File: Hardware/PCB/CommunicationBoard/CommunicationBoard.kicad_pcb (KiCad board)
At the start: 4 copper layers, 60 x 60 mm, 54 parts, among them J1 SWD, J2 Conn_01x07, J3 Conn_01x07, J4 Conn_01x07, J6 USB_C_Receptacle_USB2.0, J7 TWELITER, SW1 nRF_RESET, SW2 nRF_DFU, SW3 TWE_CLEAR, SW4 TWE_RESET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

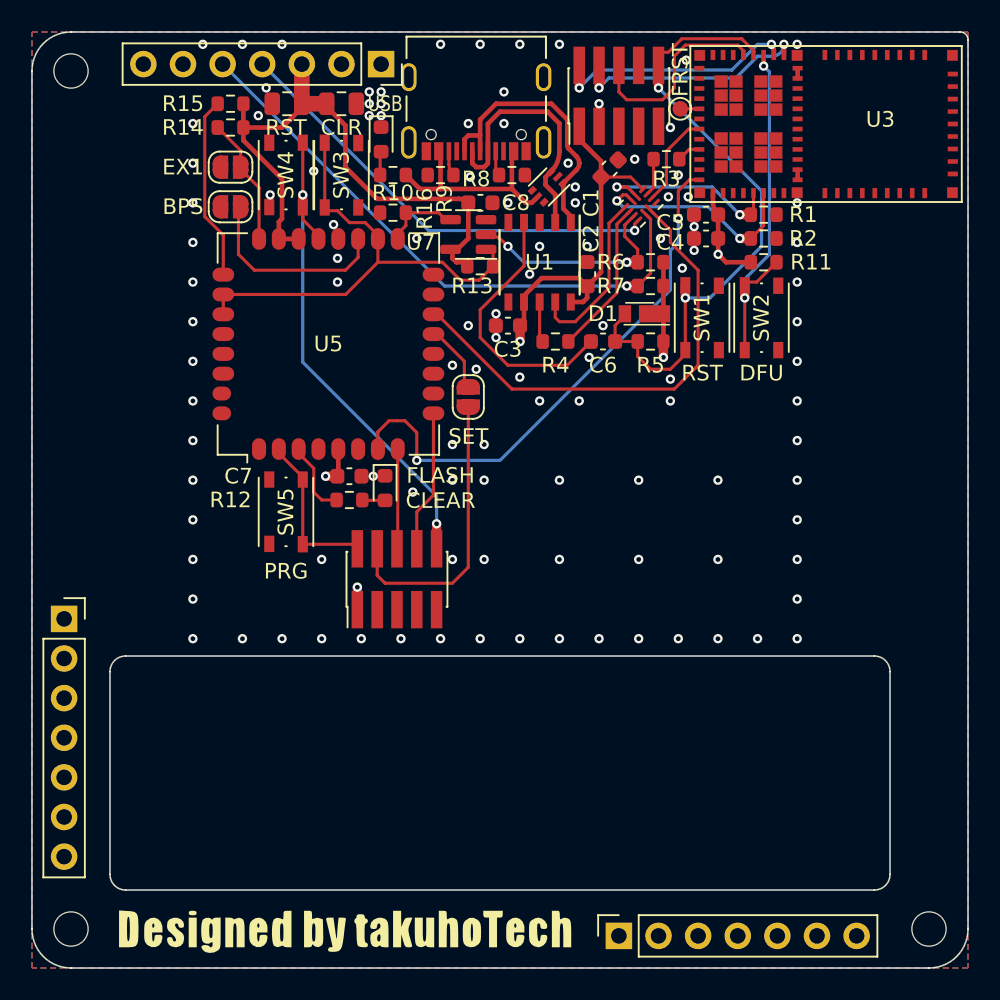
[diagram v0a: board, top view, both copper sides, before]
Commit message: 無線モジュールのビア置き終了、ひとまず完成
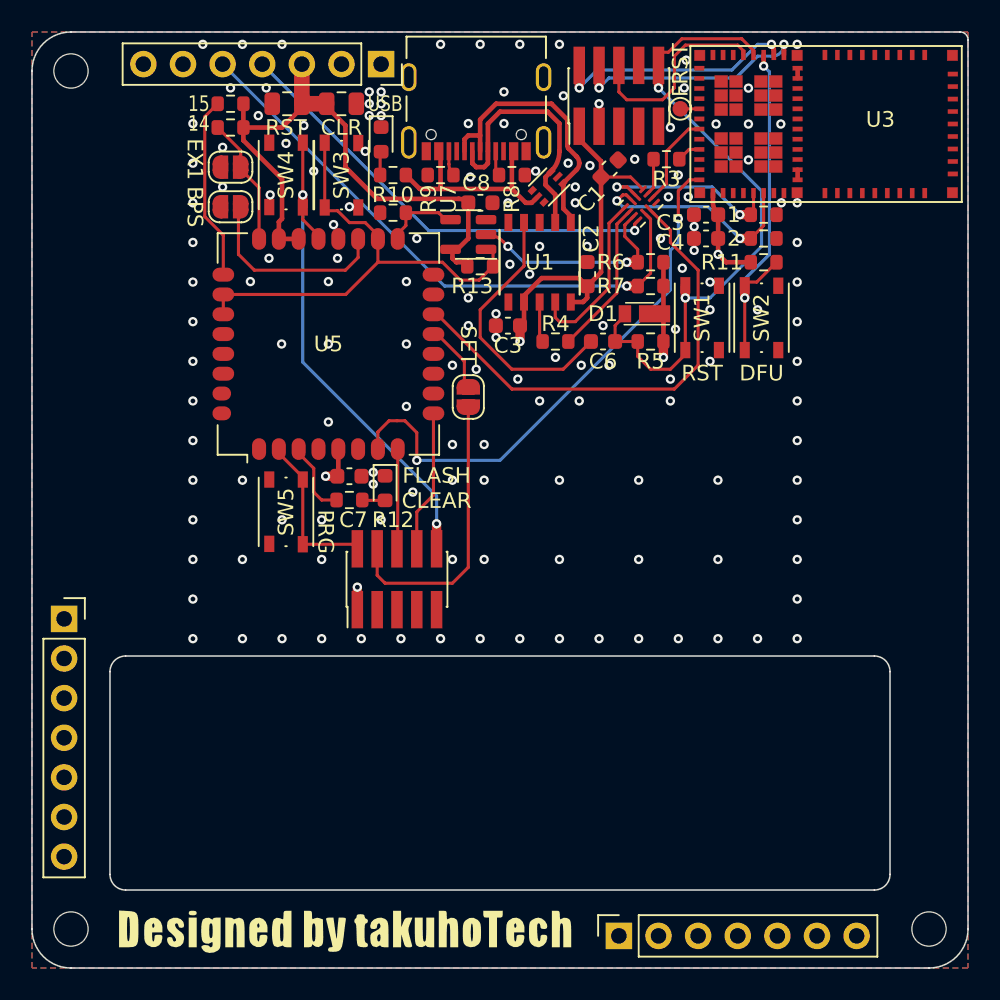
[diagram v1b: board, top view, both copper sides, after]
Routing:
- net GND: vias 111 -> 151
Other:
- board text added: "1"
- board text added: "14"
- board text added: "15"
- board text added: "2"
- board text added: "3V3"
- board text added: "GND"
- board text added: "NC"
- board text added: "RXIN"
- board text added: "TXOUT"

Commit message: Add MediaBoard
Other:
- board text added: "MEM CLR"
- board text removed: "FLASH CLEAR"
- board text removed: "LoRaアンテナのゲインの回転軸"
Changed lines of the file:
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@@
     (grid_origin 145 100)
     (pcbplotparams
-      (layerselection 0x00010a0_7ffffff8)
+      (layerselection 0x00010fc_ffffffff)
       (disableapertmacros false)
-      (usegerberextensions false)
-      (usegerberattributes true)
-      (usegerberadvancedattributes true)
-      (creategerberjobfile true)
+      (usegerberextensions true)
+      (usegerberattributes false)
+      (usegerberadvancedattributes false)
+      (creategerberjobfile false)
       (svguseinch false)
       (svgprecision 6)
-      (excludeedgelayer false)
+      (excludeedgelayer true)
       (plotframeref false)
       (viasonmask false)
       (mode 1)
-      (useauxorigin false)
+      (useauxorigin true)
       (hpglpennumber 1)
       (hpglpenspeed 20)
@@
       (plotinvisibletext false)
       (sketchpadsonfab false)
-      (subtractmaskfromsilk false)
-      (outputformat 5)
+      (subtractmaskfromsilk true)
+      (outputformat 1)
       (mirror false)
       (drillshape 0)
       (scaleselection 1)
-      (outputdirectory "")
+      (outputdirectory "gerber/")
     )
   )
@@
     (property "Sheetname" "")
     (attr smd)
-    (fp_text reference "C6" (at 0 1.27) (layer "F.SilkS")
+    (fp_text reference "C6" (at -1.905 -1.143) (layer "F.SilkS")
       (effects (font (size 1 1) (thickness 0.15)))
     )
@@
     (property "Sheetname" "")
     (attr smd)
-    (fp_text reference "R4" (at 0 -1.143) (layer "F.SilkS")
+    (fp_text reference "R4" (at -0.762 -1.143) (layer "F.SilkS")
       (effects (font (size 1 1) (thickness 0.15)))
     )
@@
     (property "Sheetname" "")
     (attr smd)
-    (fp_text reference "D1" (at 2.352 0) (layer "F.SilkS")
+    (fp_text reference "D1" (at 2.352 0.762) (layer "F.SilkS") hide
       (effects (font (size 1 1) (thickness 0.15)))
     )
@@
     (property "Sheetname" "")
     (attr smd)
-    (fp_text reference "R11" (at -2.676 0) (layer "F.SilkS")
+    (fp_text reference "R11" (at -2.676 0) (layer "F.SilkS") hide
       (effects (font (size 1 1) (thickness 0.15)))
     )
@@
     (property "Sheetname" "")
     (attr smd)
-    (fp_text reference "R5" (at 0 -1.27) (layer "F.SilkS")
+    (fp_text reference "R5" (at 3.048 1.143) (layer "F.SilkS")
       (effects (font (size 1 1) (thickness 0.15)))
     )
@@
     )
   )
-  (gr_line (start 181 74) (end 181 71.5) (layer "Dwgs.User") (width 0.15))
-  (gr_line (start 175 75) (end 190 75) (layer "Dwgs.User") (width 0.15))
-  (gr_line (start 181 76) (end 181 78.5) (layer "Dwgs.User") (width 0.15))
-  (gr_line (start 181 71.5) (end 181.5 73) (layer "Dwgs.User") (width 0.15))
   (gr_line (start 164.4 70.3) (end 160.7 70.3) (layer "Dwgs.User") (width 0.05))
-  (gr_line (start 181 78.5) (end 181.5 77) (layer "Dwgs.User") (width 0.15))
-  (gr_line (start 181 71.5) (end 180.5 73) (layer "Dwgs.User") (width 0.15))
-  (gr_line (start 181 78.5) (end 180.5 77) (layer "Dwgs.User") (width 0.15))
   (gr_arc (start 174.5 70) (mid 174.853553 70.146447) (end 175 70.5) (layer "Edge.Cuts") (width 0.1))
   (gr_arc (start 115 72.5) (mid 115.732233 70.732233) (end 117.5 70) (layer "Edge.Cuts") (width 0.1))
@@
     (effects (font (size 1 1) (thickness 0.15)))
   )
-  (gr_text "DFU" (at 161.764 91.872) (layer "F.SilkS")
-    (effects (font (size 1 1) (thickness 0.15)))
+  (gr_text "DFU" (at 159.478 84.76) (layer "F.SilkS")
+    (effects (font (size 1 0.8) (thickness 0.15)))
   )
   (gr_text "CLR" (at 134.84 76.124) (layer "F.SilkS")
     (effects (font (size 1 1) (thickness 0.15)))
   )
-  (gr_text "RST" (at 157.954 91.872) (layer "F.SilkS")
-    (effects (font (size 1 1) (thickness 0.15)))
+  (gr_text "RST" (at 157.192 84.76) (layer "F.SilkS")
+    (effects (font (size 1 0.8) (thickness 0.15)))
   )
   (gr_text "BPS" (at 125.442 81.204 270) (layer "F.SilkS")
     (effects (font (size 1 1) (thickness 0.15)))
   )
-  (gr_text "FLASH\nCLEAR" (at 140.936 99.238) (layer "F.SilkS")
+  (gr_text "MEM\nCLR" (at 139.92 99.238 270) (layer "F.SilkS")
     (effects (font (size 1 1) (thickness 0.15)))
   )
@@
     (effects (font (size 1 0.8) (thickness 0.15)))
   )
-  (gr_text "LoRaアンテナのゲインの回転軸" (at 191 73) (layer "Cmts.User")
-    (effects (font (size 1 1) (thickness 0.15)))
-  )
   (via (at 155.795 80.569) (size 0.6) (drill 0.3) (layers "F.Cu" "B.Cu") (free) (net 1))
